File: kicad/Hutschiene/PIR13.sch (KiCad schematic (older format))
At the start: 24 parts, among them P301 CONN_PIR_OG, P302 CONN_PIR_EG, P303 CONN_PIR_UG, Q301 IRLML2502, Q302 IRLML2502, Q303 IRLML2502

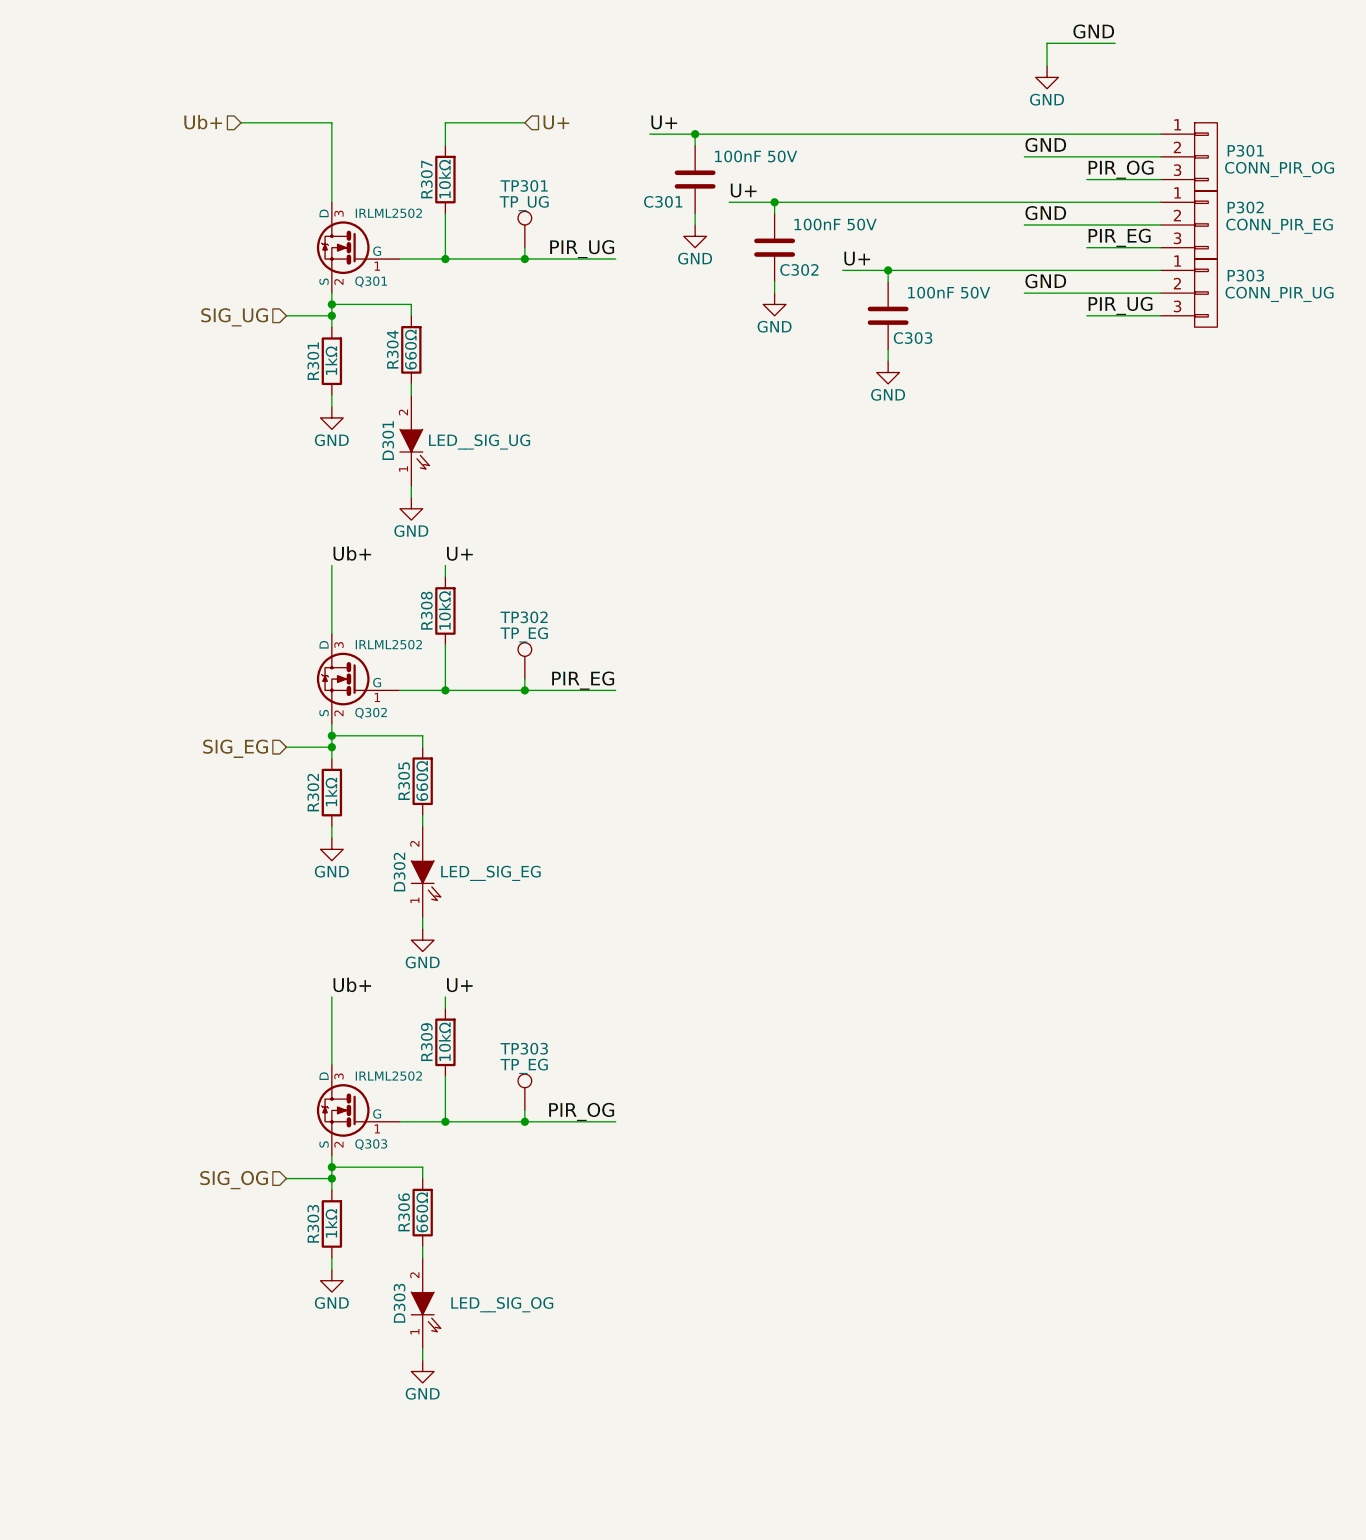
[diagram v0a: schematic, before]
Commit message: Continuing with the Hutschiene design and layout
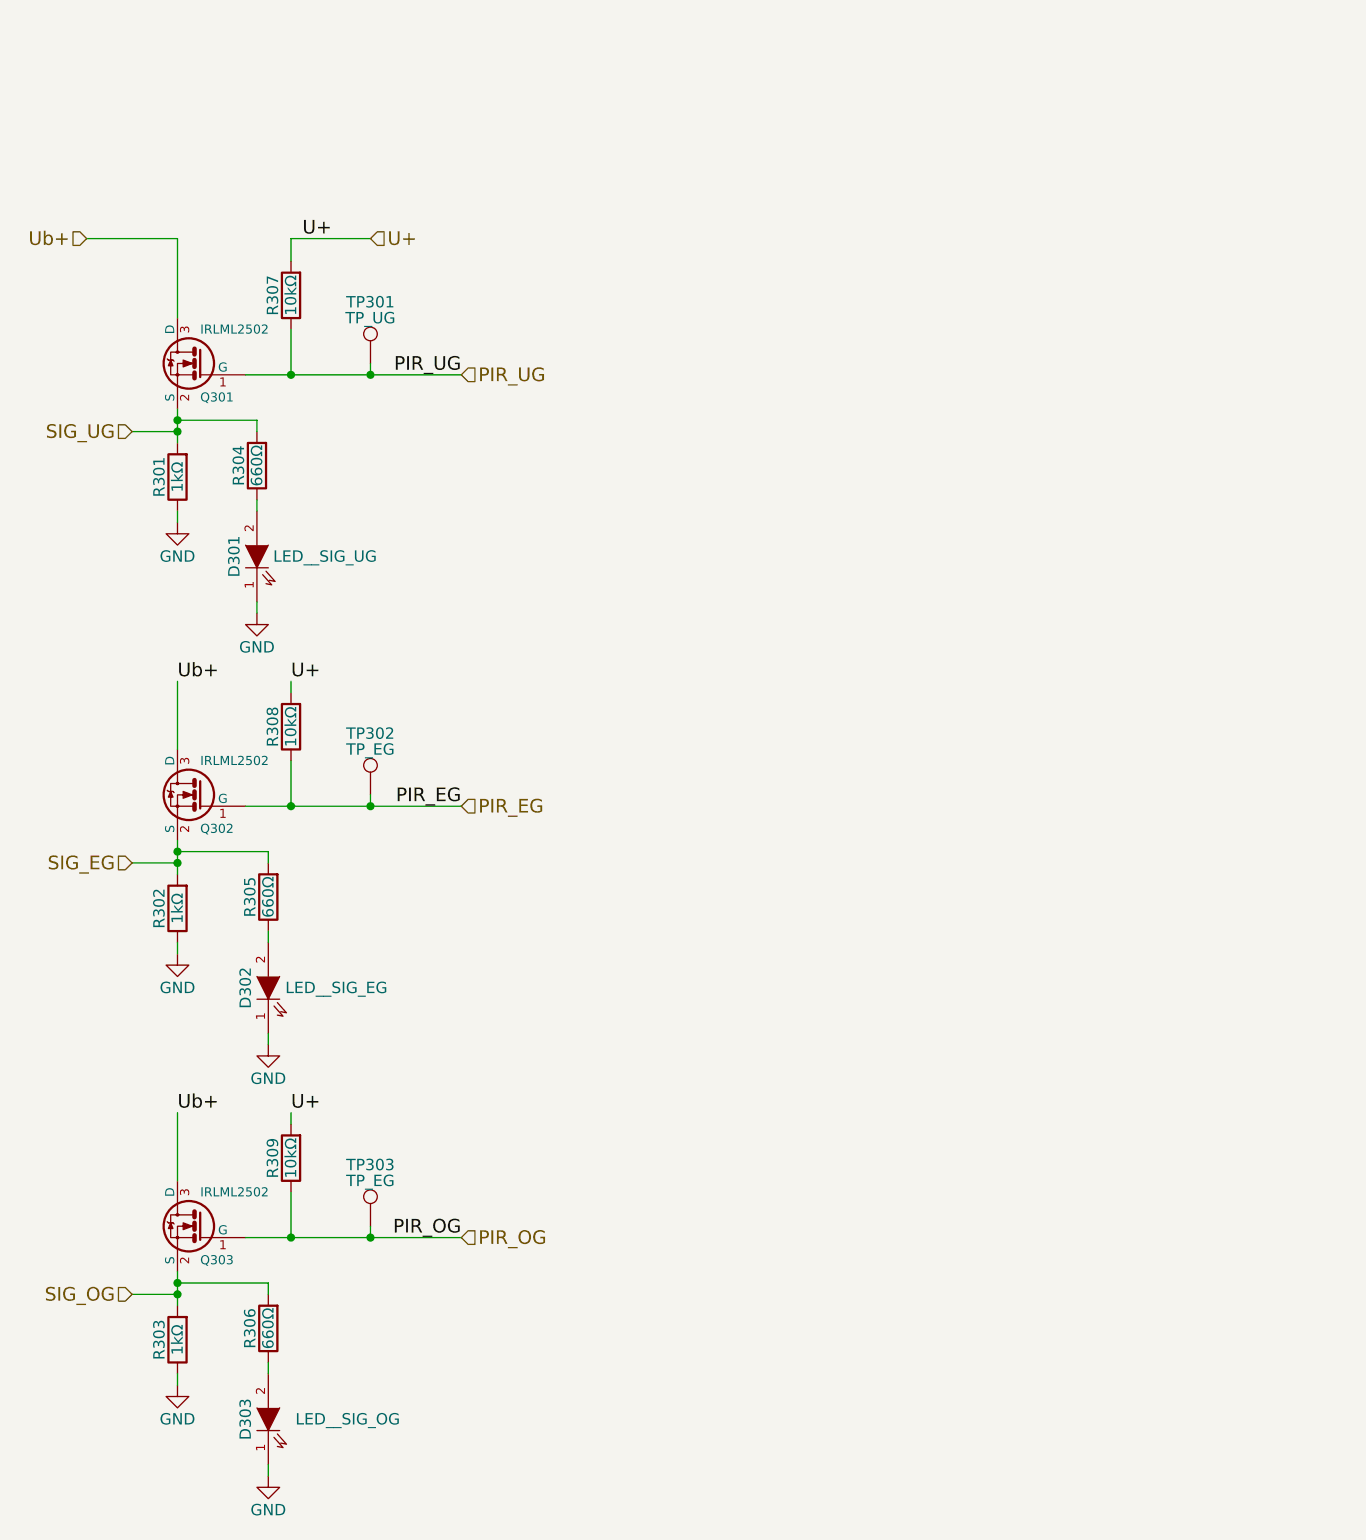
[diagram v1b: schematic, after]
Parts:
- removed C301, C302, C303: 100nF 50V, Capacitors_SMD:C_0805, symbol C
- removed P301: CONN_PIR_OG, tl2c-footprint:PCB_Screw_Terminal_Block_5mm_x_3, symbol CONN_01X03
- removed P302: CONN_PIR_EG, tl2c-footprint:PCB_Screw_Terminal_Block_5mm_x_3, symbol CONN_01X03
- removed P303: CONN_PIR_UG, tl2c-footprint:PCB_Screw_Terminal_Block_5mm_x_3, symbol CONN_01X03
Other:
- moved on the sheet: D301, D302, D303, Q301, Q302, Q303, R301, R302, R303, R304, R305, R306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

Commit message: Further work on the redesign
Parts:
- removed D301: LED__SIG_UG, LEDs:LED_0805, symbol LED
- removed D302: LED__SIG_EG, LEDs:LED_0805, symbol LED
- removed D303: LED__SIG_OG, LEDs:LED_0805, symbol LED
- removed R304, R305, R306: 660Ω, Resistors_SMD:R_0805, symbol R
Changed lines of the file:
@@
 Ub+
 $Comp
-L GND #PWR022
+L GND #PWR021
 U 1 1 585215A4
 P 1720 3160
-F 0 "#PWR022" H 1720 2910 50  0001 C CNN
+F 0 "#PWR021" H 1720 2910 50  0001 C CNN
 F 1 "GND" H 1720 3010 50  0000 C CNN
 F 2 "" H 1720 3160 50  0000 C CNN
@@
 PIR_EG
 $Comp
-L GND #PWR023
+L GND #PWR022
 U 1 1 58521B24
 P 1720 5060
-F 0 "#PWR023" H 1720 4810 50  0001 C CNN
+F 0 "#PWR022" H 1720 4810 50  0001 C CNN
 F 1 "GND" H 1720 4910 50  0000 C CNN
 F 2 "" H 1720 5060 50  0000 C CNN
@@
 PIR_OG
 $Comp
-L GND #PWR024
+L GND #PWR023
 U 1 1 58521C75
 P 1720 6960
-F 0 "#PWR024" H 1720 6710 50  0001 C CNN
+F 0 "#PWR023" H 1720 6710 50  0001 C CNN
 F 1 "GND" H 1720 6810 50  0000 C CNN
 F 2 "" H 1720 6960 50  0000 C CNN
@@
 Text HLabel 1520 6560 0    60   Input ~ 0
 SIG_OG
-$Comp
-L LED D301
-U 1 1 5852C267
-P 2070 3310
-F 0 "D301" H 2070 3410 50  0000 C CNN
-F 1 "LED__SIG_UG" V 2070 3010 50  0000 C CNN
-F 2 "LEDs:LED_0805" H 2070 3310 50  0001 C CNN
-F 3 "" H 2070 3310 50  0000 C CNN
-	1    2070 3310
-	0    -1   -1   0
-$EndComp
-$Comp
-L R R304
-U 1 1 5852C57E
-P 2070 2910
-F 0 "R304" V 2150 2910 50  0000 C CNN
-F 1 "660Ω" V 2070 2910 50  0000 C CNN
-F 2 "Resistors_SMD:R_0805" V 2000 2910 50  0001 C CNN
-F 3 "" H 2070 2910 50  0000 C CNN
-	1    2070 2910
-	-1   0    0    1
-$EndComp
-$Comp
-L LED D302
-U 1 1 5852CAA2
-P 2120 5210
-F 0 "D302" H 2120 5310 50  0000 C CNN
-F 1 "LED__SIG_EG" V 2120 4910 50  0000 C CNN
-F 2 "LEDs:LED_0805" H 2120 5210 50  0001 C CNN
-F 3 "" H 2120 5210 50  0000 C CNN
-	1    2120 5210
-	0    -1   -1   0
-$EndComp
-$Comp
-L R R305
-U 1 1 5852CAA8
-P 2120 4810
-F 0 "R305" V 2200 4810 50  0000 C CNN
-F 1 "660Ω" V 2120 4810 50  0000 C CNN
-F 2 "Resistors_SMD:R_0805" V 2050 4810 50  0001 C CNN
-F 3 "" H 2120 4810 50  0000 C CNN
-	1    2120 4810
-	-1   0    0    1
-$EndComp
-$Comp
-L GND #PWR025
-U 1 1 5852CAAF
-P 2120 5460
-F 0 "#PWR025" H 2120 5210 50  0001 C CNN
-F 1 "GND" H 2120 5310 50  0000 C CNN
-F 2 "" H 2120 5460 50  0000 C CNN
-F 3 "" H 2120 5460 50  0000 C CNN
-	1    2120 5460
-	1    0    0    -1
-$EndComp
-$Comp
-L LED D303
-U 1 1 5852D26A
-P 2120 7110
-F 0 "D303" H 2120 7210 50  0000 C CNN
-F 1 "LED__SIG_OG" V 2120 6760 50  0000 C CNN
-F 2 "LEDs:LED_0805" H 2120 7110 50  0001 C CNN
-F 3 "" H 2120 7110 50  0000 C CNN
-	1    2120 7110
-	0    -1   -1   0
-$EndComp
-$Comp
-L R R306
-U 1 1 5852D270
-P 2120 6710
-F 0 "R306" V 2200 6710 50  0000 C CNN
-F 1 "660Ω" V 2120 6710 50  0000 C CNN
-F 2 "Resistors_SMD:R_0805" V 2050 6710 50  0001 C CNN
-F 3 "" H 2120 6710 50  0000 C CNN
-	1    2120 6710
-	-1   0    0    1
-$EndComp
-$Comp
-L GND #PWR026
-U 1 1 5852D277
-P 2120 7360
-F 0 "#PWR026" H 2120 7110 50  0001 C CNN
-F 1 "GND" H 2120 7210 50  0000 C CNN
-F 2 "" H 2120 7360 50  0000 C CNN
-F 3 "" H 2120 7360 50  0000 C CNN
-	1    2120 7360
-	1    0    0    -1
-$EndComp
 $Comp
 L TEST_1P TP301
@@
 $EndComp
 Wire Wire Line
-	2020 2510 2220 2510
-Wire Wire Line
-	2220 2510 2570 2510
-Wire Wire Line
-	2570 2510 2970 2510
+	2020 2510 2970 2510
 Wire Wire Line
 	2220 2510 2220 2310
@@
 	1720 2760 1520 2760
 Wire Wire Line
-	1720 2660 1720 2710
-Wire Wire Line
-	1720 2710 1720 2760
-Wire Wire Line
-	1720 2760 1720 2810
+	1720 2660 1720 2810
 Connection ~ 1720 2760
 Wire Wire Line
-	2020 4410 2220 4410
-Wire Wire Line
-	2220 4410 2570 4410
-Wire Wire Line
-	2570 4410 2970 4410
+	2020 4410 2970 4410
 Wire Wire Line
 	2220 4410 2220 4210
@@
 	1720 4660 1520 4660
 Wire Wire Line
-	1720 4560 1720 4610
-Wire Wire Line
-	1720 4610 1720 4660
-Wire Wire Line
-	1720 4660 1720 4710
+	1720 4560 1720 4710
 Connection ~ 1720 4660
 Wire Wire Line
-	2020 6310 2220 6310
-Wire Wire Line
-	2220 6310 2570 6310
-Wire Wire Line
-	2570 6310 2970 6310
+	2020 6310 2970 6310
 Wire Wire Line
 	2220 6310 2220 6110
@@
 	1720 6560 1520 6560
 Wire Wire Line
-	1720 6460 1720 6510
-Wire Wire Line
-	1720 6510 1720 6560
-Wire Wire Line
-	1720 6560 1720 6610
+	1720 6460 1720 6610
 Connection ~ 1720 6560
-Wire Wire Line
-	2070 3510 2070 3560
-Wire Wire Line
-	2120 5410 2120 5460
-Wire Wire Line
-	2120 4660 2120 4610
-Wire Wire Line
-	2120 4610 1720 4610
-Connection ~ 1720 4610
-Wire Wire Line
-	2120 7310 2120 7360
-Wire Wire Line
-	2120 6560 2120 6510
-Wire Wire Line
-	2120 6510 1720 6510
-Connection ~ 1720 6510
 Wire Wire Line
 	2570 1910 2220 1910
@@
 Connection ~ 2570 6310
 Wire Wire Line
-	2070 2760 2070 2710
-Wire Wire Line
-	2070 2710 1720 2710
-Connection ~ 1720 2710
-$Comp
-L GND #PWR030
-U 1 1 5852C6FF
-P 2070 3560
-F 0 "#PWR030" H 2070 3310 50  0001 C CNN
-F 1 "GND" H 2070 3410 50  0000 C CNN
-F 2 "" H 2070 3560 50  0000 C CNN
-F 3 "" H 2070 3560 50  0000 C CNN
-	1    2070 3560
-	1    0    0    -1
-$EndComp
-Wire Wire Line
 	1720 1910 1720 2260
 Wire Wire Line
 	2220 1910 2220 2010
-Wire Wire Line
-	2070 3060 2070 3110
-Wire Wire Line
-	2120 4960 2120 5010
-Wire Wire Line
-	2120 6860 2120 6910
 Text HLabel 2970 6310 2    60   Input ~ 0
 PIR_OG

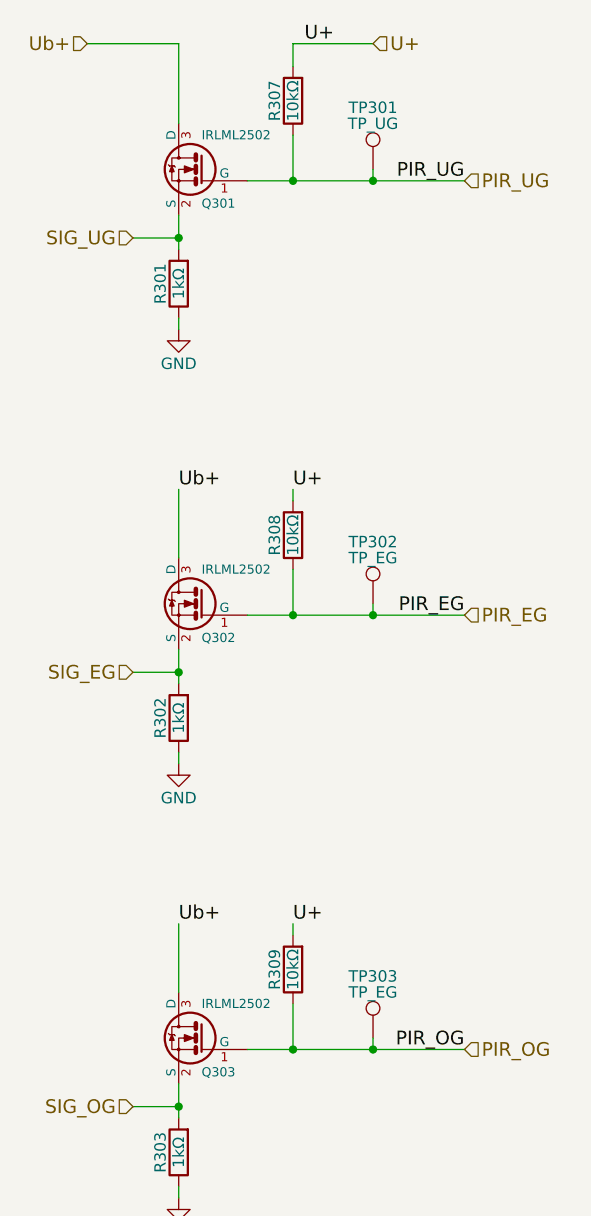
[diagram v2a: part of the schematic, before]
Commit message: Further work on the new Hutschiene Layout
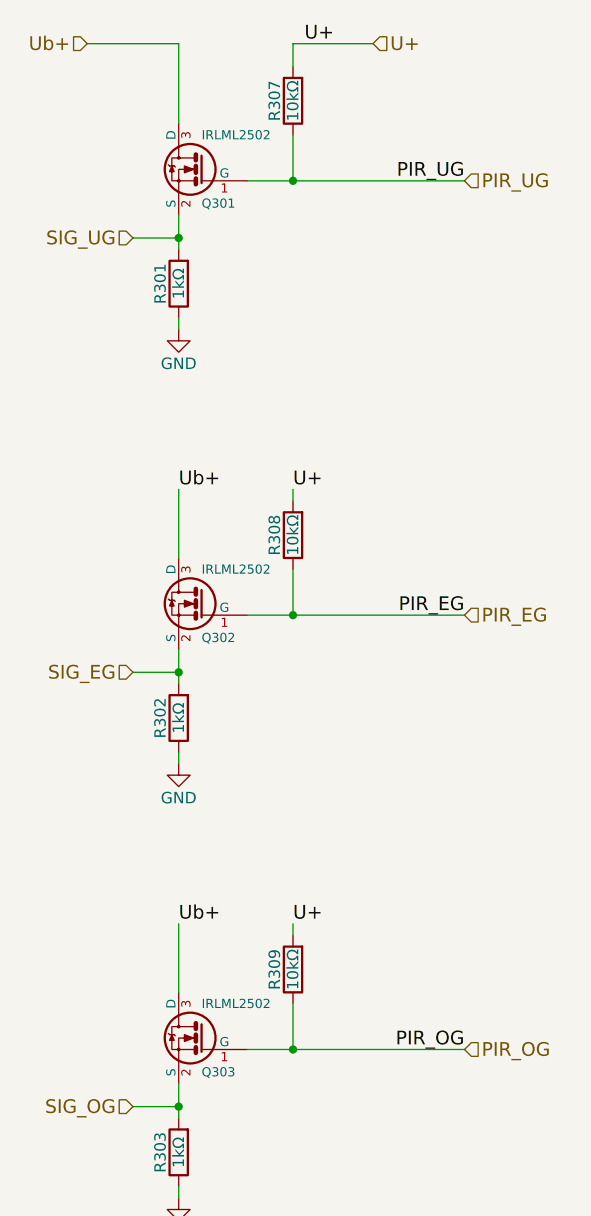
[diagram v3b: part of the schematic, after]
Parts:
- removed TP301: TP_UG, Measurement_Points:Measurement_Point_Round-SMD-Pad_Small, symbol TEST_1P
- removed TP302, TP303: TP_EG, Measurement_Points:Measurement_Point_Round-SMD-Pad_Small, symbol TEST_1P
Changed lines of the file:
@@
 Ub+
 $Comp
-L GND #PWR021
+L GND #PWR020
 U 1 1 585215A4
 P 1720 3160
-F 0 "#PWR021" H 1720 2910 50  0001 C CNN
+F 0 "#PWR020" H 1720 2910 50  0001 C CNN
 F 1 "GND" H 1720 3010 50  0000 C CNN
 F 2 "" H 1720 3160 50  0000 C CNN
@@
 PIR_EG
 $Comp
-L GND #PWR022
+L GND #PWR021
 U 1 1 58521B24
 P 1720 5060
-F 0 "#PWR022" H 1720 4810 50  0001 C CNN
+F 0 "#PWR021" H 1720 4810 50  0001 C CNN
 F 1 "GND" H 1720 4910 50  0000 C CNN
 F 2 "" H 1720 5060 50  0000 C CNN
@@
 PIR_OG
 $Comp
-L GND #PWR023
+L GND #PWR022
 U 1 1 58521C75
 P 1720 6960
-F 0 "#PWR023" H 1720 6710 50  0001 C CNN
+F 0 "#PWR022" H 1720 6710 50  0001 C CNN
 F 1 "GND" H 1720 6810 50  0000 C CNN
 F 2 "" H 1720 6960 50  0000 C CNN
@@
 Text HLabel 1520 6560 0    60   Input ~ 0
 SIG_OG
-$Comp
-L TEST_1P TP301
-U 1 1 58533CA9
-P 2570 2460
-F 0 "TP301" H 2570 2730 50  0000 C CNN
-F 1 "TP_UG" H 2570 2660 50  0000 C CNN
-F 2 "Measurement_Points:Measurement_Point_Round-SMD-Pad_Small" H 2770 2460 50  0001 C CNN
-F 3 "" H 2770 2460 50  0000 C CNN
-	1    2570 2460
-	1    0    0    -1
-$EndComp
-$Comp
-L TEST_1P TP302
-U 1 1 58533E0F
-P 2570 4360
-F 0 "TP302" H 2570 4630 50  0000 C CNN
-F 1 "TP_EG" H 2570 4560 50  0000 C CNN
-F 2 "Measurement_Points:Measurement_Point_Round-SMD-Pad_Small" H 2770 4360 50  0001 C CNN
-F 3 "" H 2770 4360 50  0000 C CNN
-	1    2570 4360
-	1    0    0    -1
-$EndComp
-$Comp
-L TEST_1P TP303
-U 1 1 58534405
-P 2570 6260
-F 0 "TP303" H 2570 6530 50  0000 C CNN
-F 1 "TP_EG" H 2570 6460 50  0000 C CNN
-F 2 "Measurement_Points:Measurement_Point_Round-SMD-Pad_Small" H 2770 6260 50  0001 C CNN
-F 3 "" H 2770 6260 50  0000 C CNN
-	1    2570 6260
-	1    0    0    -1
-$EndComp
 Wire Wire Line
 	2020 2510 2970 2510
@@
 	2570 1910 2220 1910
 Wire Wire Line
-	2570 2460 2570 2510
-Connection ~ 2570 2510
-Wire Wire Line
-	2570 4360 2570 4410
-Connection ~ 2570 4410
-Wire Wire Line
-	2570 6260 2570 6310
-Connection ~ 2570 6310
-Wire Wire Line
 	1720 1910 1720 2260
